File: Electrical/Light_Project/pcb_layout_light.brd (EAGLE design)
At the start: 22.8 x 18.7 mm, 9 parts, among them U1 REG710NA-3.3/3K, U2 ATTINY85V-10SU, U3 FSM8JRT

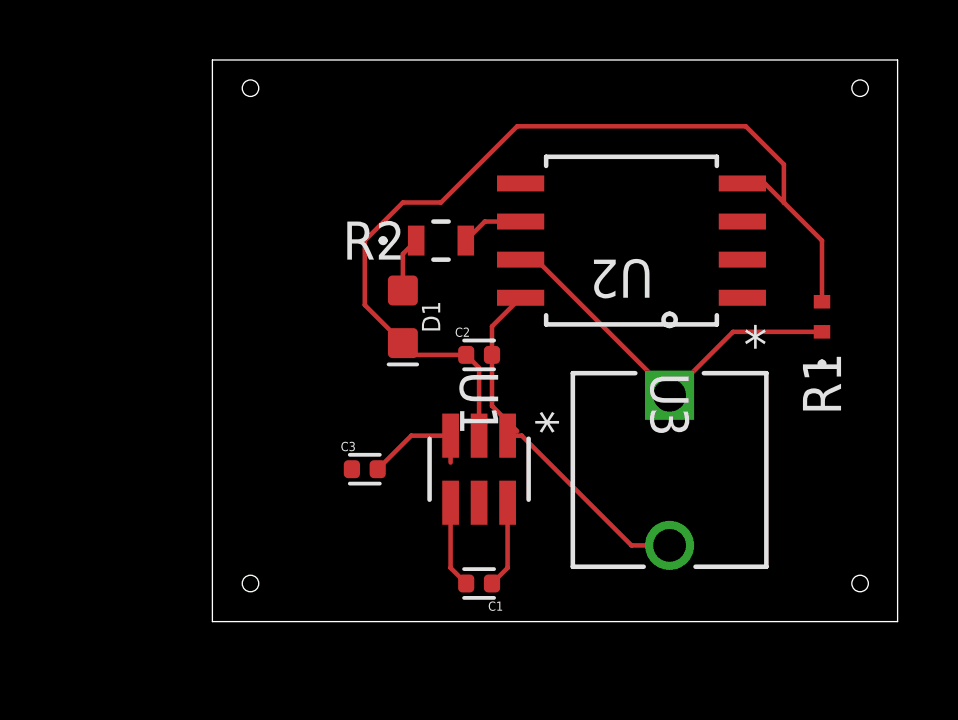
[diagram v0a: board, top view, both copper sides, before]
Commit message: add updated solidwords files with screws and nuts
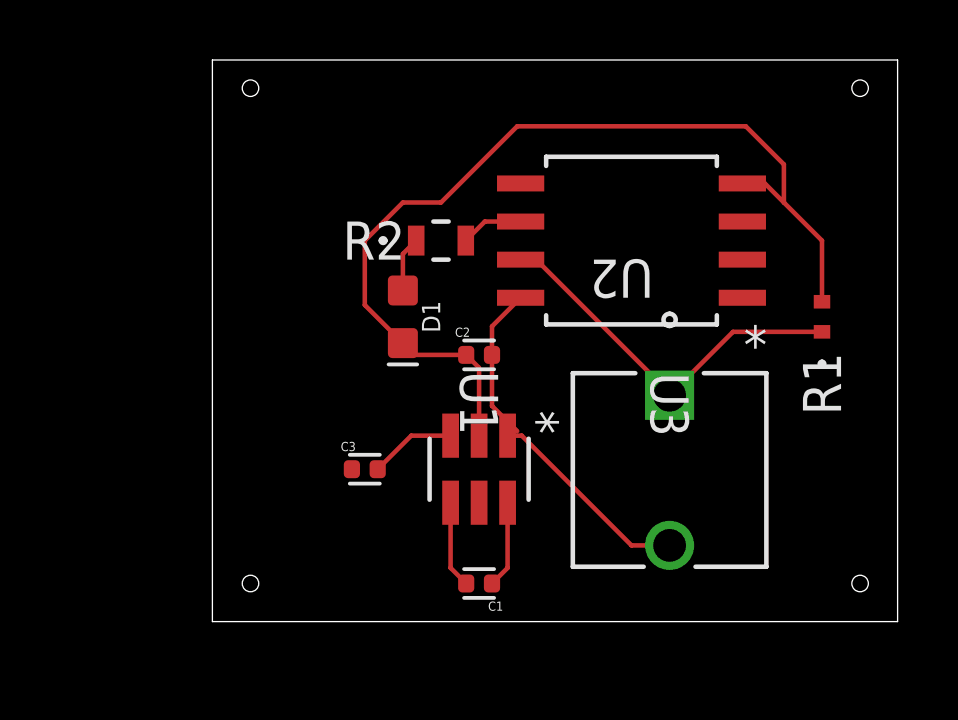
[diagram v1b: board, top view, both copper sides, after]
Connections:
- net VCC renamed N$8
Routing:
- net N$4: track 3.79 -> 2.89 mm
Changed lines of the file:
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@@
 <hole x="46.99" y="0" drill="0.55"/>
 <hole x="26.67" y="0" drill="0.55"/>
+<dimension x1="26.67" y1="17.78" x2="46.99" y2="17.78" x3="36.83" y3="19.05" textsize="1.778" layer="1" dtype="diameter"/>
+<dimension x1="27.94" y1="16.51" x2="27.94" y2="0" x3="22.86" y3="8.255" textsize="1.778" layer="1" dtype="diameter"/>
+<dimension x1="40.64" y1="3.81" x2="48.26" y2="3.81" x3="44.45" y3="24.13" textsize="1.778" layer="1" dtype="diameter"/>
+<dimension x1="40.64" y1="3.81" x2="40.64" y2="-1.27" x3="52.07" y3="1.27" textsize="1.778" layer="1" dtype="diameter"/>
+<dimension x1="31.75" y1="8.89" x2="25.4" y2="8.89" x3="28.575" y3="24.13" textsize="1.778" layer="1"/>
+<dimension x1="31.75" y1="8.89" x2="31.75" y2="17.78" x3="10.16" y3="13.335" textsize="1.778" layer="1"/>
 </plain>
 <attributes>
@@
 <param name="RoutingGrid" value="50mil"/>
 <param name="AutoGrid" value="1"/>
-<param name="Efforts" value="0"/>
+<param name="Efforts" value="2"/>
 <param name="TopRouterVariant" value="1"/>
 <param name="tpViaShape" value="round"/>
@@
 <contactref element="U1" pad="3"/>
 <contactref element="C3" pad="2"/>
-<wire x1="33.34" y1="4.0316875" x2="33.34" y2="4.9276" width="0.1524" layer="1"/>
 <wire x1="30.91" y1="3.81" x2="32.0276" y2="4.9276" width="0.1524" layer="1"/>
 <wire x1="32.0276" y1="4.9276" x2="33.34" y2="4.9276" width="0.1524" layer="1"/>
-<wire x1="33.34" y1="4.0316875" x2="34.29" y2="2.6924" width="0" layer="19" extent="1-1"/>
+<wire x1="33.34" y1="4.9276" x2="34.29" y2="2.6924" width="0" layer="19" extent="1-1"/>
 </signal>
 <signal name="N$5">
@@
 <wire x1="33.34" y1="0.52" x2="33.86" y2="0" width="0.1524" layer="1"/>
 </signal>
-<signal name="VCC">
-<contactref element="C3" pad="1"/>
-</signal>
 <signal name="N$6">
 <contactref element="D1" pad="A"/>
@@
 <wire x1="34.4816" y1="12.065" x2="35.6743" y2="12.065" width="0.1524" layer="1"/>
 </signal>
+<signal name="N$8">
+<contactref element="C3" pad="1"/>
+</signal>
 </signals>

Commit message: change route width
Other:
- board size 22.8 x 18.7 mm -> 22.8 x 20 mm
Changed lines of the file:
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@@
 <board>
 <plain>
-<wire x1="25.4" y1="-1.27" x2="48.24" y2="-1.27" width="0" layer="20"/>
-<wire x1="48.24" y1="-1.27" x2="48.24" y2="17.45" width="0" layer="20"/>
+<wire x1="25.4" y1="-2.54" x2="48.24" y2="-2.54" width="0" layer="20"/>
+<wire x1="48.24" y1="-2.54" x2="48.24" y2="17.45" width="0" layer="20"/>
 <wire x1="48.24" y1="17.45" x2="25.4" y2="17.45" width="0" layer="20"/>
-<wire x1="25.4" y1="17.45" x2="25.4" y2="-1.27" width="0" layer="20"/>
-<hole x="46.99" y="16.51" drill="0.55"/>
-<hole x="26.67" y="16.51" drill="0.55"/>
-<hole x="46.99" y="0" drill="0.55"/>
-<hole x="26.67" y="0" drill="0.55"/>
-<dimension x1="26.67" y1="17.78" x2="46.99" y2="17.78" x3="36.83" y3="19.05" textsize="1.778" layer="1" dtype="diameter"/>
-<dimension x1="27.94" y1="16.51" x2="27.94" y2="0" x3="22.86" y3="8.255" textsize="1.778" layer="1" dtype="diameter"/>
-<dimension x1="40.64" y1="3.81" x2="48.26" y2="3.81" x3="44.45" y3="24.13" textsize="1.778" layer="1" dtype="diameter"/>
-<dimension x1="40.64" y1="3.81" x2="40.64" y2="-1.27" x3="52.07" y3="1.27" textsize="1.778" layer="1" dtype="diameter"/>
-<dimension x1="31.75" y1="8.89" x2="25.4" y2="8.89" x3="28.575" y3="24.13" textsize="1.778" layer="1"/>
-<dimension x1="31.75" y1="8.89" x2="31.75" y2="17.78" x3="10.16" y3="13.335" textsize="1.778" layer="1"/>
+<wire x1="25.4" y1="17.45" x2="25.4" y2="-2.54" width="0" layer="20"/>
+<hole x="46.355" y="15.24" drill="1.65"/>
+<hole x="27.94" y="15.24" drill="1.65"/>
+<hole x="46.355" y="-0.635" drill="1.65"/>
+<hole x="27.94" y="-0.635" drill="1.65"/>
+<dimension x1="25.4" y1="-2.54" x2="48.24" y2="-2.54" x3="36.82" y3="-5.08" textsize="1.778" layer="1" dtype="diameter"/>
+<dimension x1="25.4" y1="17.78" x2="25.4" y2="-2.54" x3="17.78" y3="7.62" textsize="1.778" layer="1" dtype="diameter"/>
 </plain>
 <attributes>
@@
 <contactref element="C2" pad="1"/>
 <contactref element="D1" pad="C"/>
-<wire x1="43.0657" y1="13.335" x2="43.815" y2="13.335" width="0.1524" layer="1"/>
-<wire x1="43.815" y1="13.335" x2="44.45" y2="12.7" width="0.1524" layer="1"/>
-<wire x1="44.45" y1="12.7" x2="45.72" y2="11.43" width="0.1524" layer="1"/>
-<wire x1="45.72" y1="11.43" x2="45.72" y2="9.3916" width="0.1524" layer="1"/>
-<wire x1="31.75" y1="8.013" x2="32.143" y2="7.62" width="0.1524" layer="1"/>
-<wire x1="32.143" y1="7.62" x2="33.86" y2="7.62" width="0.1524" layer="1"/>
-<wire x1="33.86" y1="7.62" x2="34.29" y2="7.19" width="0.1524" layer="1"/>
-<wire x1="34.29" y1="7.19" x2="34.29" y2="4.9276" width="0.1524" layer="1"/>
-<wire x1="44.45" y1="12.7" x2="44.45" y2="13.97" width="0.1524" layer="1"/>
-<wire x1="44.45" y1="13.97" x2="43.18" y2="15.24" width="0.1524" layer="1"/>
-<wire x1="43.18" y1="15.24" x2="35.56" y2="15.24" width="0.1524" layer="1"/>
-<wire x1="35.56" y1="15.24" x2="33.02" y2="12.7" width="0.1524" layer="1"/>
-<wire x1="33.02" y1="12.7" x2="31.75" y2="12.7" width="0.1524" layer="1"/>
-<wire x1="31.75" y1="12.7" x2="30.48" y2="11.43" width="0.1524" layer="1"/>
-<wire x1="30.48" y1="11.43" x2="30.48" y2="9.283" width="0.1524" layer="1"/>
-<wire x1="30.48" y1="9.283" x2="31.75" y2="8.013" width="0.1524" layer="1"/>
+<wire x1="43.0657" y1="13.335" x2="43.815" y2="13.335" width="0.3048" layer="1"/>
+<wire x1="43.815" y1="13.335" x2="44.45" y2="12.7" width="0.3048" layer="1"/>
+<wire x1="44.45" y1="12.7" x2="45.72" y2="11.43" width="0.3048" layer="1"/>
+<wire x1="45.72" y1="11.43" x2="45.72" y2="9.3916" width="0.3048" layer="1"/>
+<wire x1="31.75" y1="8.013" x2="32.143" y2="7.62" width="0.3048" layer="1"/>
+<wire x1="32.143" y1="7.62" x2="33.86" y2="7.62" width="0.3048" layer="1"/>
+<wire x1="33.86" y1="7.62" x2="34.29" y2="7.19" width="0.3048" layer="1"/>
+<wire x1="34.29" y1="7.19" x2="34.29" y2="4.9276" width="0.3048" layer="1"/>
+<wire x1="44.45" y1="12.7" x2="44.45" y2="13.97" width="0.3048" layer="1"/>
+<wire x1="44.45" y1="13.97" x2="43.18" y2="15.24" width="0.3048" layer="1"/>
+<wire x1="43.18" y1="15.24" x2="35.56" y2="15.24" width="0.3048" layer="1"/>
+<wire x1="35.56" y1="15.24" x2="33.02" y2="12.7" width="0.3048" layer="1"/>
+<wire x1="33.02" y1="12.7" x2="31.75" y2="12.7" width="0.3048" layer="1"/>
+<wire x1="31.75" y1="12.7" x2="30.48" y2="11.43" width="0.3048" layer="1"/>
+<wire x1="30.48" y1="11.43" x2="30.48" y2="9.283" width="0.3048" layer="1"/>
+<wire x1="30.48" y1="9.283" x2="31.75" y2="8.013" width="0.3048" layer="1"/>
 </signal>
 <signal name="N$1">
@@
 <contactref element="U3" pad="2"/>
 <contactref element="C2" pad="2"/>
-<wire x1="35.24" y1="4.9276" x2="35.7124" y2="4.9276" width="0.1524" layer="1"/>
-<wire x1="39.37" y1="1.27" x2="40.64" y2="1.27" width="0.1524" layer="1"/>
-<wire x1="35.7124" y1="4.9276" x2="39.37" y2="1.27" width="0.1524" layer="1"/>
-<wire x1="34.72" y1="7.62" x2="34.72" y2="5.92" width="0.1524" layer="1"/>
-<wire x1="34.72" y1="5.92" x2="35.4076" y2="5.2324" width="0.1524" layer="1"/>
-<wire x1="35.4076" y1="5.2324" x2="35.56" y2="5.08" width="0.1524" layer="1"/>
-<wire x1="34.72" y1="7.62" x2="34.72" y2="8.5707" width="0.1524" layer="1"/>
-<wire x1="34.72" y1="8.5707" x2="35.6743" y2="9.525" width="0.1524" layer="1"/>
-<wire x1="35.3568" y1="5.0292" x2="35.3568" y2="5.1816" width="0.1524" layer="1"/>
-<wire x1="35.3568" y1="5.1816" x2="35.4076" y2="5.2324" width="0.1524" layer="1"/>
-<wire x1="35.3568" y1="5.0292" x2="35.24" y2="4.9276" width="0.1524" layer="1"/>
+<wire x1="35.24" y1="4.9276" x2="35.7124" y2="4.9276" width="0.3048" layer="1"/>
+<wire x1="39.37" y1="1.27" x2="40.64" y2="1.27" width="0.3048" layer="1"/>
+<wire x1="35.7124" y1="4.9276" x2="39.37" y2="1.27" width="0.3048" layer="1"/>
+<wire x1="35.4076" y1="5.2324" x2="35.56" y2="5.08" width="0.3048" layer="1"/>
+<wire x1="34.72" y1="8.5707" x2="35.6743" y2="9.525" width="0.3048" layer="1"/>
+<wire x1="35.3568" y1="5.0292" x2="35.3568" y2="5.1816" width="0.3048" layer="1"/>
+<wire x1="35.3568" y1="5.1816" x2="35.4076" y2="5.2324" width="0.3048" layer="1"/>
+<wire x1="35.3568" y1="5.0292" x2="35.24" y2="4.9276" width="0.3048" layer="1"/>
+<wire x1="34.72" y1="7.62" x2="34.72" y2="8.5707" width="0.3048" layer="1"/>
+<wire x1="35.24" y1="4.9276" x2="35.56" y2="6.35" width="0.3048" layer="1"/>
+<wire x1="35.56" y1="6.35" x2="34.72" y2="7.62" width="0.3048" layer="1"/>
 </signal>
 <signal name="N$4">
@@
 <contactref element="U1" pad="3"/>
 <contactref element="C3" pad="2"/>
-<wire x1="30.91" y1="3.81" x2="32.0276" y2="4.9276" width="0.1524" layer="1"/>
-<wire x1="32.0276" y1="4.9276" x2="33.34" y2="4.9276" width="0.1524" layer="1"/>
+<wire x1="30.91" y1="3.81" x2="32.0276" y2="4.9276" width="0.3048" layer="1"/>
+<wire x1="32.0276" y1="4.9276" x2="33.34" y2="4.9276" width="0.3048" layer="1"/>
 <wire x1="33.34" y1="4.9276" x2="34.29" y2="2.6924" width="0" layer="19" extent="1-1"/>
 </signal>
@@
 <contactref element="R1" pad="1"/>
 <contactref element="U2" pad="7"/>
-<wire x1="40.64" y1="6.2738" x2="40.6781" y2="6.3119" width="0.1524" layer="1"/>
-<wire x1="40.6781" y1="6.3119" x2="42.7546" y2="8.3884" width="0.1524" layer="1"/>
-<wire x1="42.7546" y1="8.3884" x2="45.72" y2="8.3884" width="0.1524" layer="1"/>
-<wire x1="35.6743" y1="10.795" x2="36.195" y2="10.795" width="0.1524" layer="1"/>
-<wire x1="36.195" y1="10.795" x2="40.6781" y2="6.3119" width="0.1524" layer="1"/>
+<wire x1="40.64" y1="6.2738" x2="40.6781" y2="6.3119" width="0.3048" layer="1"/>
+<wire x1="40.6781" y1="6.3119" x2="42.7546" y2="8.3884" width="0.3048" layer="1"/>
+<wire x1="42.7546" y1="8.3884" x2="45.72" y2="8.3884" width="0.3048" layer="1"/>
+<wire x1="35.6743" y1="10.795" x2="36.195" y2="10.795" width="0.3048" layer="1"/>
+<wire x1="36.195" y1="10.795" x2="40.6781" y2="6.3119" width="0.3048" layer="1"/>
 </signal>
 <signal name="N$2">
 <contactref element="U1" pad="6"/>
 <contactref element="C1" pad="1"/>
-<wire x1="34.72" y1="0" x2="35.24" y2="0.52" width="0.1524" layer="1"/>
-<wire x1="35.24" y1="0.52" x2="35.24" y2="2.6924" width="0.1524" layer="1"/>
+<wire x1="34.72" y1="0" x2="35.24" y2="0.52" width="0.3048" layer="1"/>
+<wire x1="35.24" y1="0.52" x2="35.24" y2="2.6924" width="0.3048" layer="1"/>
 </signal>
 <signal name="N$3">
 <contactref element="U1" pad="4"/>
 <contactref element="C1" pad="2"/>
-<wire x1="33.34" y1="2.6924" x2="33.34" y2="0.52" width="0.1524" layer="1"/>
-<wire x1="33.34" y1="0.52" x2="33.86" y2="0" width="0.1524" layer="1"/>
+<wire x1="33.34" y1="2.6924" x2="33.34" y2="0.52" width="0.3048" layer="1"/>
+<wire x1="33.34" y1="0.52" x2="33.86" y2="0" width="0.3048" layer="1"/>
 </signal>
 <signal name="N$6">
 <contactref element="D1" pad="A"/>
 <contactref element="R2" pad="1"/>
-<wire x1="31.75" y1="9.767" x2="31.75" y2="10.9866" width="0.1524" layer="1"/>
-<wire x1="31.75" y1="10.9866" x2="32.1934" y2="11.43" width="0.1524" layer="1"/>
+<wire x1="31.75" y1="9.767" x2="31.75" y2="10.9866" width="0.3048" layer="1"/>
+<wire x1="31.75" y1="10.9866" x2="32.1934" y2="11.43" width="0.3048" layer="1"/>
 </signal>
 <signal name="N$7">
 <contactref element="R2" pad="2"/>
 <contactref element="U2" pad="6"/>
-<wire x1="33.8466" y1="11.43" x2="34.4816" y2="12.065" width="0.1524" layer="1"/>
-<wire x1="34.4816" y1="12.065" x2="35.6743" y2="12.065" width="0.1524" layer="1"/>
+<wire x1="33.8466" y1="11.43" x2="34.4816" y2="12.065" width="0.3048" layer="1"/>
+<wire x1="34.4816" y1="12.065" x2="35.6743" y2="12.065" width="0.3048" layer="1"/>
 </signal>
 <signal name="N$8">

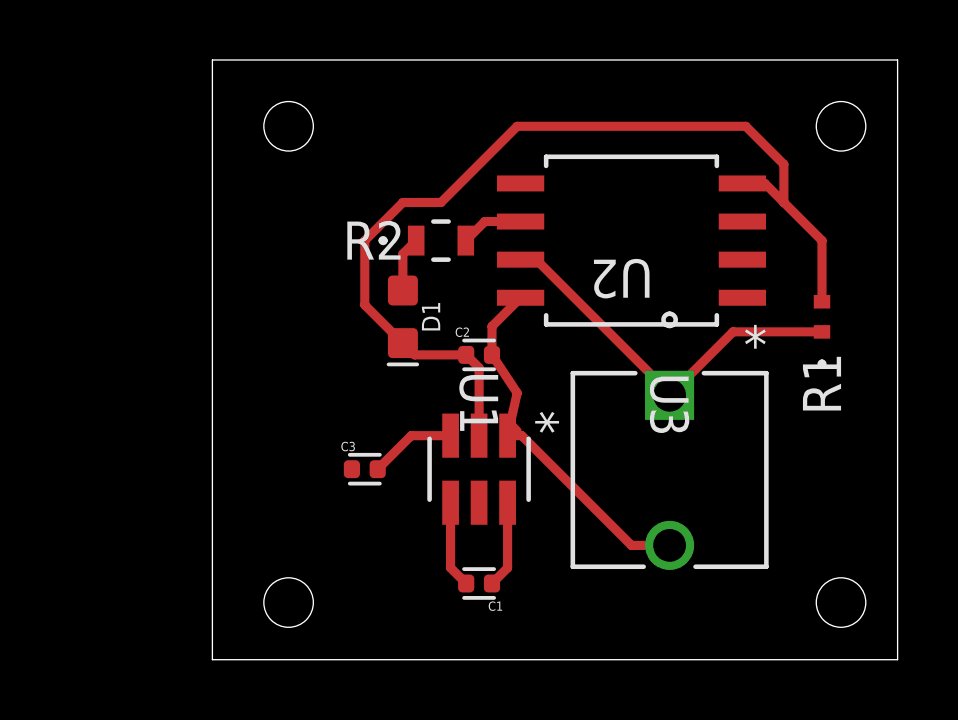
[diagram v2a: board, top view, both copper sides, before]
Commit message: Update bypass cap to go to ground and add header pins for switch and power supply
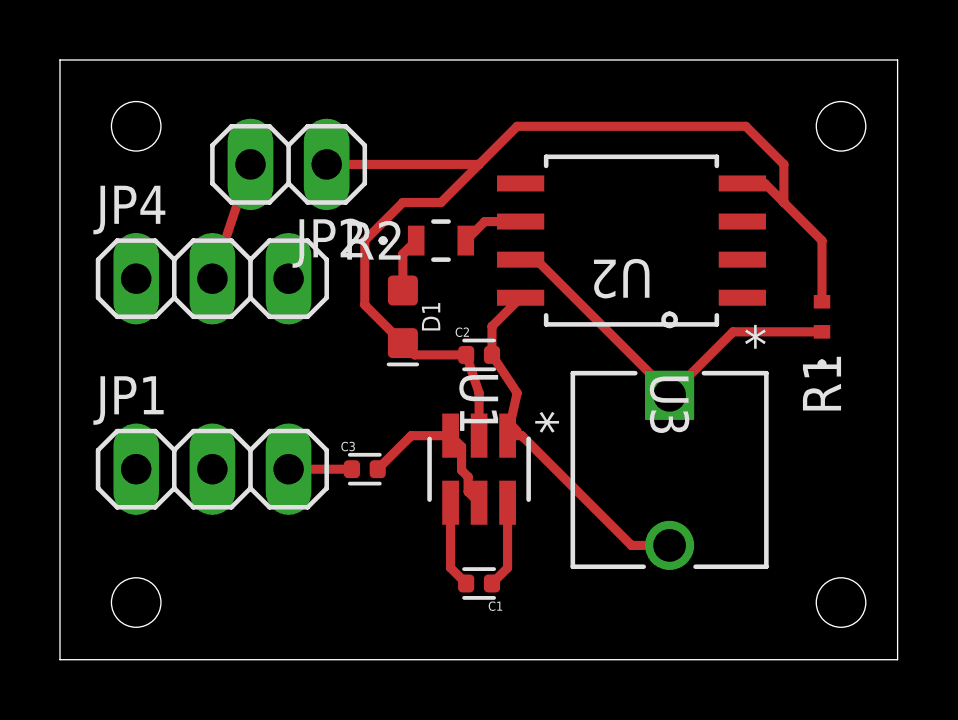
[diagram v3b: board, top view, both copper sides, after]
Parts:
- added JP1, JP4: (no value), pinhead:1X03
- added JP2: (no value), pinhead:1X02
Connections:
- new net N$10: JP2.2, JP4.2
- net GND: now also JP2.1
- net N$8: now also JP1.3
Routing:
- net GND: track 31.9 -> 36.7 mm
- net N$10: track 0.00 -> 4.02 mm
- net N$4: track 2.89 -> 5.52 mm
- net N$8: track 0.00 -> 2.11 mm
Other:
- board size 22.8 x 20 mm -> 27.9 x 20 mm
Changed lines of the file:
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@@
 <board>
 <plain>
-<wire x1="25.4" y1="-2.54" x2="48.24" y2="-2.54" width="0" layer="20"/>
+<wire x1="20.32" y1="-2.54" x2="48.24" y2="-2.54" width="0" layer="20"/>
 <wire x1="48.24" y1="-2.54" x2="48.24" y2="17.45" width="0" layer="20"/>
-<wire x1="48.24" y1="17.45" x2="25.4" y2="17.45" width="0" layer="20"/>
-<wire x1="25.4" y1="17.45" x2="25.4" y2="-2.54" width="0" layer="20"/>
+<wire x1="48.24" y1="17.45" x2="20.32" y2="17.45" width="0" layer="20"/>
+<wire x1="20.32" y1="17.45" x2="20.32" y2="-2.54" width="0" layer="20"/>
 <hole x="46.355" y="15.24" drill="1.65"/>
-<hole x="27.94" y="15.24" drill="1.65"/>
+<hole x="22.86" y="15.24" drill="1.65"/>
 <hole x="46.355" y="-0.635" drill="1.65"/>
-<hole x="27.94" y="-0.635" drill="1.65"/>
+<hole x="22.86" y="-0.635" drill="1.65"/>
 <dimension x1="25.4" y1="-2.54" x2="48.24" y2="-2.54" x3="36.82" y3="-5.08" textsize="1.778" layer="1" dtype="diameter"/>
 <dimension x1="25.4" y1="17.78" x2="25.4" y2="-2.54" x3="17.78" y3="7.62" textsize="1.778" layer="1" dtype="diameter"/>
@@
 <attribute name="VENDOR" value="Susumu" x="33.02" y="11.43" size="1.778" layer="27" display="off"/>
 </element>
+<element name="JP2" library="pinhead" library_urn="urn:adsk.eagle:library:325" package="1X02" package3d_urn="urn:adsk.eagle:package:22435/2" value="" x="27.94" y="13.97" smashed="yes" rot="R180">
+<attribute name="NAME" x="30.5562" y="12.1412" size="1.27" layer="25" ratio="10" rot="R180"/>
+<attribute name="VALUE" x="30.48" y="17.145" size="1.27" layer="27" rot="R180"/>
+</element>
+<element name="JP1" library="pinhead" library_urn="urn:adsk.eagle:library:325" package="1X03" package3d_urn="urn:adsk.eagle:package:22458/2" value="" x="25.4" y="3.81" smashed="yes">
+<attribute name="NAME" x="21.5138" y="5.6388" size="1.27" layer="25" ratio="10"/>
+<attribute name="VALUE" x="21.59" y="0.635" size="1.27" layer="27"/>
+</element>
+<element name="JP4" library="pinhead" library_urn="urn:adsk.eagle:library:325" package="1X03" package3d_urn="urn:adsk.eagle:package:22458/2" value="" x="25.4" y="10.16" smashed="yes">
+<attribute name="NAME" x="21.5138" y="11.9888" size="1.27" layer="25" ratio="10"/>
+<attribute name="VALUE" x="21.59" y="6.985" size="1.27" layer="27"/>
+</element>
 </elements>
 <signals>
@@
 <wire x1="31.75" y1="8.013" x2="32.143" y2="7.62" width="0.3048" layer="1"/>
 <wire x1="32.143" y1="7.62" x2="33.86" y2="7.62" width="0.3048" layer="1"/>
-<wire x1="33.86" y1="7.62" x2="34.29" y2="7.19" width="0.3048" layer="1"/>
-<wire x1="34.29" y1="7.19" x2="34.29" y2="4.9276" width="0.3048" layer="1"/>
 <wire x1="44.45" y1="12.7" x2="44.45" y2="13.97" width="0.3048" layer="1"/>
 <wire x1="44.45" y1="13.97" x2="43.18" y2="15.24" width="0.3048" layer="1"/>
 <wire x1="43.18" y1="15.24" x2="35.56" y2="15.24" width="0.3048" layer="1"/>
-<wire x1="35.56" y1="15.24" x2="33.02" y2="12.7" width="0.3048" layer="1"/>
+<wire x1="35.56" y1="15.24" x2="34.29" y2="13.97" width="0.3048" layer="1"/>
+<wire x1="34.29" y1="13.97" x2="33.02" y2="12.7" width="0.3048" layer="1"/>
 <wire x1="33.02" y1="12.7" x2="31.75" y2="12.7" width="0.3048" layer="1"/>
 <wire x1="31.75" y1="12.7" x2="30.48" y2="11.43" width="0.3048" layer="1"/>
 <wire x1="30.48" y1="11.43" x2="30.48" y2="9.283" width="0.3048" layer="1"/>
 <wire x1="30.48" y1="9.283" x2="31.75" y2="8.013" width="0.3048" layer="1"/>
+<wire x1="33.86" y1="7.62" x2="34.29" y2="6.35" width="0.3048" layer="1"/>
+<wire x1="34.29" y1="6.35" x2="34.29" y2="5.08" width="0.3048" layer="1"/>
+<contactref element="JP2" pad="1"/>
+<wire x1="29.21" y1="13.97" x2="34.29" y2="13.97" width="0.3048" layer="1"/>
+<wire x1="34.29" y1="4.9276" x2="34.29" y2="5.08" width="0" layer="19" extent="1-1"/>
 </signal>
 <signal name="N$1">
@@
 <wire x1="30.91" y1="3.81" x2="32.0276" y2="4.9276" width="0.3048" layer="1"/>
 <wire x1="32.0276" y1="4.9276" x2="33.34" y2="4.9276" width="0.3048" layer="1"/>
-<wire x1="33.34" y1="4.9276" x2="34.29" y2="2.6924" width="0" layer="19" extent="1-1"/>
+<wire x1="33.34" y1="4.9276" x2="33.7058" y2="4.5618" width="0.3048" layer="1"/>
+<wire x1="33.9242" y1="3.55525" x2="33.9242" y2="3.0582" width="0.3048" layer="1"/>
+<wire x1="33.9242" y1="3.0582" x2="34.29" y2="2.6924" width="0.3048" layer="1"/>
+<wire x1="33.7058" y1="4.5618" x2="33.7058" y2="3.77365" width="0.3048" layer="1"/>
+<wire x1="33.7058" y1="3.77365" x2="33.9242" y2="3.55525" width="0.3048" layer="1"/>
 </signal>
 <signal name="N$5">
@@
 <signal name="N$8">
 <contactref element="C3" pad="1"/>
+<contactref element="JP1" pad="3"/>
+<wire x1="27.94" y1="3.81" x2="30.05" y2="3.81" width="0.3048" layer="1"/>
+</signal>
+<signal name="N$10">
+<contactref element="JP2" pad="2"/>
+<contactref element="JP4" pad="2"/>
+<wire x1="25.4" y1="10.16" x2="26.67" y2="13.97" width="0.3048" layer="1"/>
 </signal>
 </signals>
